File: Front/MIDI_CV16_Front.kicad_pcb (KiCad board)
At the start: 2 copper layers, 59.5 x 128.5 mm, 23 parts, among them J1 Screw_Terminal_01x01, J10 Conn_01x01, J11 Conn_01x01, J12 Conn_01x01, J13 Conn_01x01, J14 Conn_01x01, J15 Conn_01x01, J16 Conn_01x01, J17 Conn_01x01, J18 Conn_01x01, J19 Conn_01x01, J2 Screw_Terminal_01x01, J20 Conn_01x01, J21 Conn_01x01, J22 Conn_01x01, J23 Conn_01x01, J3 Screw_Terminal_01x01, J4 Screw_Terminal_01x01, J5 Conn_01x01, J6 Conn_01x01, J7 Conn_01x01, J8 Conn_01x01, J9 Conn_01x01

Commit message: Fix DRC errors
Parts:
- J1, J2, J3, J4: footprint CustomLib:Wide_M3 -> Custom_FP:Wide_M3
- J10, J11, J5: footprint CustomLib:TactileHole -> Custom_FP:TactileHole
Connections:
- J1 pad 1: (no net) -> Net-(J1-Pad1)
- J2 pad 1: (no net) -> Net-(J2-Pad1)
- J3 pad 1: (no net) -> Net-(J3-Pad1)
- J4 pad 1: (no net) -> Net-(J4-Pad1)

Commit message: Update front panel
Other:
- net class Default removed
- board text added: "2"
- board text added: "M IDI CV16"
- board text removed: "MIDIBUS CV16"

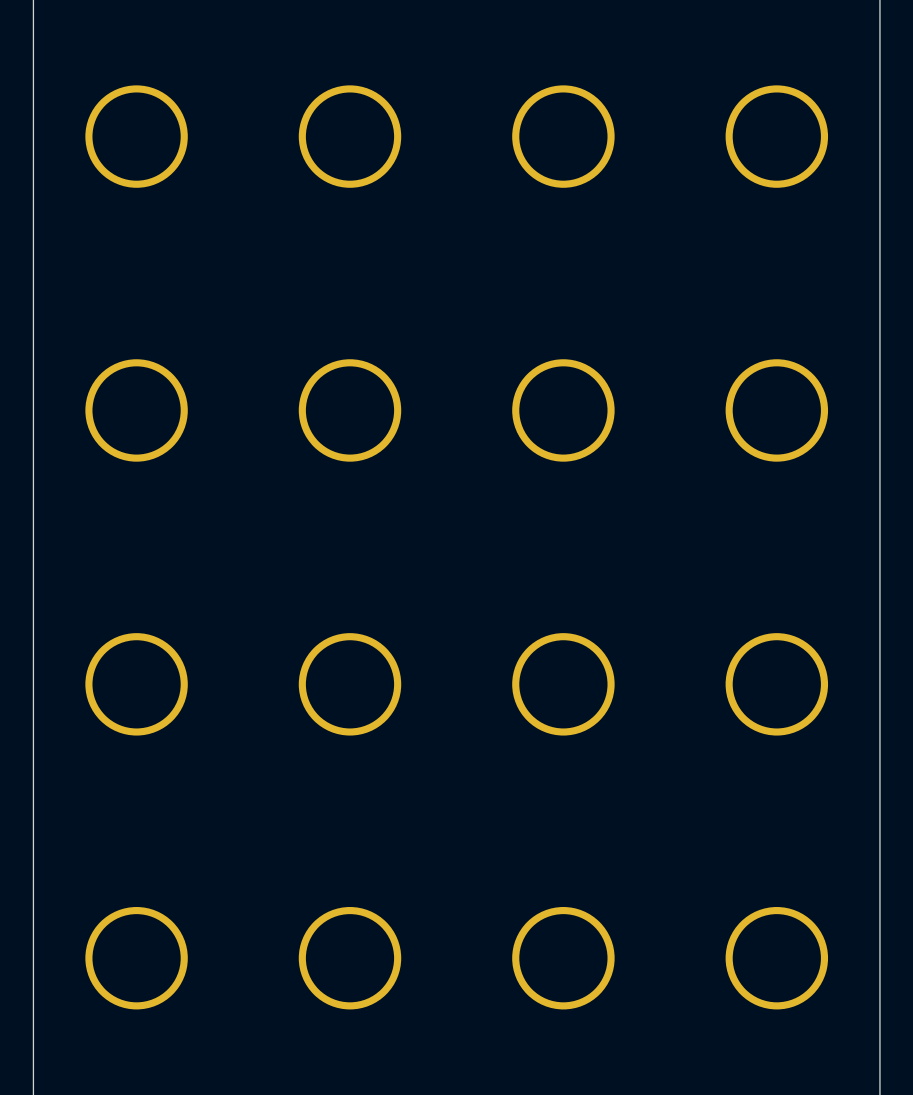
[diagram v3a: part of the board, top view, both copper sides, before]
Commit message: Fix front panel DRC
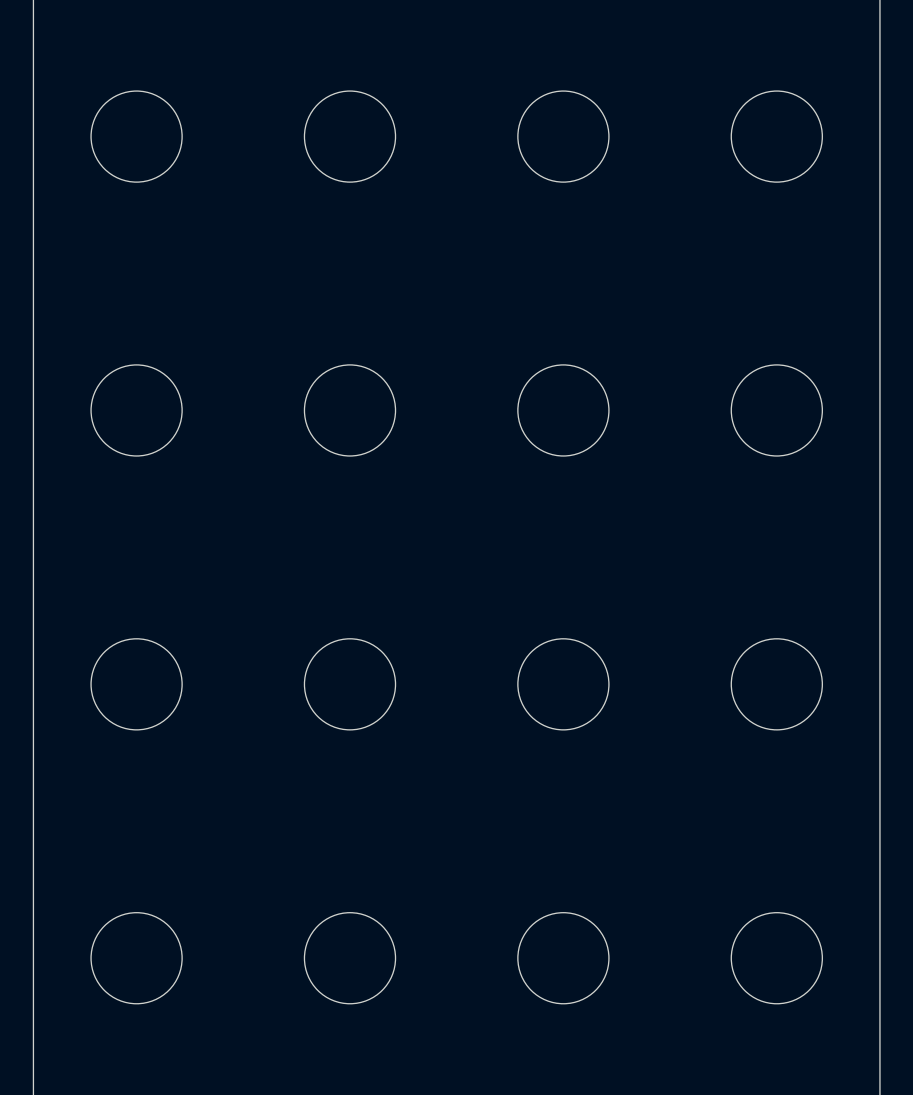
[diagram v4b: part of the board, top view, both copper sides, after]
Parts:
- J12, J13, J14, J15, J16, J17, J18, J19, J20, J21, J22, J23, J6, J7, J8, J9: footprint MountingHole:MountingHole_6.2mm_M6 -> MountingHole:MountingHole_6.4mm_M6
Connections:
- J1 pad 1: Net-(J1-Pad1) -> unconnected-(J1-Pin_1-Pad1)
- J2 pad 1: Net-(J2-Pad1) -> unconnected-(J2-Pin_1-Pad1)
- J3 pad 1: Net-(J3-Pad1) -> unconnected-(J3-Pin_1-Pad1)
- J4 pad 1: Net-(J4-Pad1) -> unconnected-(J4-Pin_1-Pad1)

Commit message: Maybe actually fix drc
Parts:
- J12, J13, J14, J15, J16, J17, J18, J19, J20, J21, J22, J23, J6, J7, J8, J9: footprint MountingHole:MountingHole_6.4mm_M6 -> Custom_FP:JackHole_3.5mm

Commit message: Finalize module
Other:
- board size 59.5 x 128.5 mm -> 60.6 x 128.5 mm
- rule pad_to_mask_clearance: 0.05 -> 0
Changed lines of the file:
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@@
   )
   (setup
-    (pad_to_mask_clearance 0.05)
+    (pad_to_mask_clearance 0)
     (pcbplotparams
       (layerselection 0x00010f0_ffffffff)
@@
       (psnegative false)
       (psa4output false)
-      (plotreference true)
+      (plotreference false)
       (plotvalue false)
       (plotinvisibletext false)
@@
       (drillshape 0)
       (scaleselection 1)
-      (outputdirectory "Gerbers/Front/")
+      (outputdirectory "outputs/")
     )
   )
@@
   (gr_line (start 67.75 72.5) (end 67.75 51.25)
     (stroke (width 0.15) (type solid)) (layer "Dwgs.User"))
-  (gr_line (start 50.25 35.5) (end 50.25 164)
+  (gr_line (start 49.7 35.5) (end 49.7 164)
     (stroke (width 0.05) (type solid)) (layer "Edge.Cuts"))
-  (gr_line (start 109.75 35.5) (end 50.25 35.5)
+  (gr_line (start 110.3 35.5) (end 49.7 35.5)
     (stroke (width 0.05) (type solid)) (layer "Edge.Cuts"))
-  (gr_line (start 109.75 164) (end 109.75 35.5)
+  (gr_line (start 110.3 164) (end 110.3 35.5)
     (stroke (width 0.05) (type solid)) (layer "Edge.Cuts"))
-  (gr_line (start 50.25 164) (end 109.75 164)
+  (gr_line (start 49.7 164) (end 110.3 164)
     (stroke (width 0.05) (type solid)) (layer "Edge.Cuts"))
   (gr_text "JLCJLCJLCJLC" (at 80 154) (layer "B.SilkS")
